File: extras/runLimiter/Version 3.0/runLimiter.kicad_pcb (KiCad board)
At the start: 2 copper layers, 70 x 50 mm, 19 parts, among them J1 5-20 Volts, J2 Vout, J3 Dry Contacts, K1 Relay, Q1 2N3904, Q2 2SD2023, U1 MCP1700-330, U2 ESP8266-01s

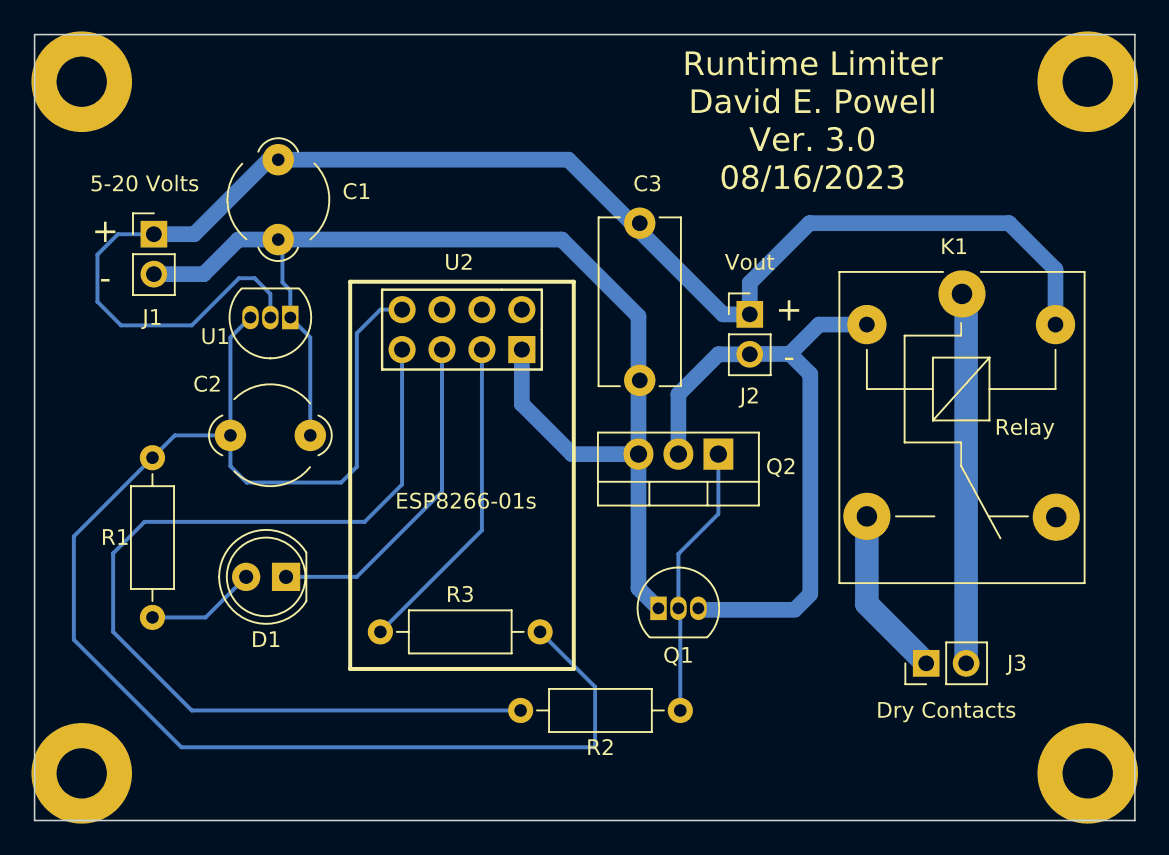
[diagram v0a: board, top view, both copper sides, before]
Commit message: Changes to board and schematic
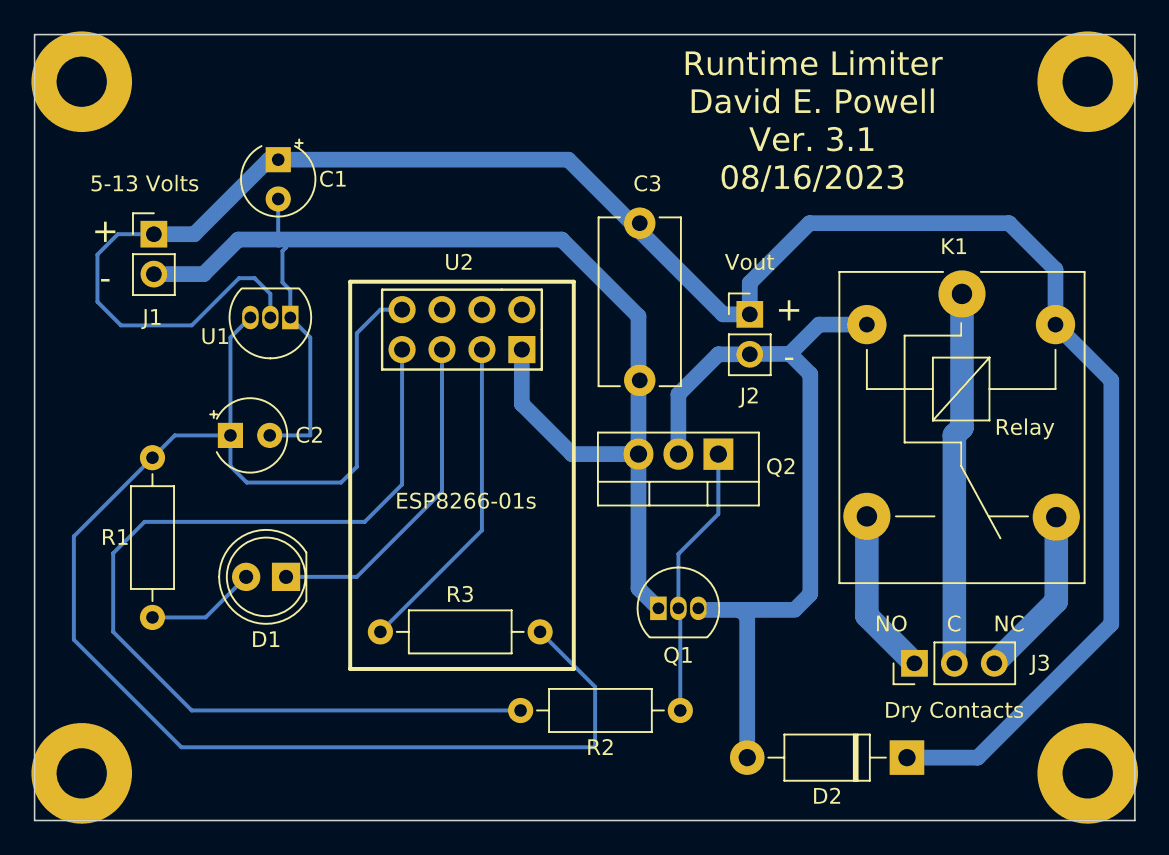
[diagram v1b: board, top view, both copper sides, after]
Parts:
- added D2: 1N4003, Diode_THT:D_DO-41_SOD81_P10.16mm_Horizontal, F.Cu at (55.5, 46.0)
- C1, C2: footprint Ferrite_THT:LairdTech_28C0236-0JW-10 -> Capacitor_THT:CP_Radial_Tantal_D4.5mm_P2.50mm
- J1: value 5-20 Volts -> 5-13 Volts
- J3: footprint Connector_PinHeader_2.54mm:PinHeader_1x02_P2.54mm_Vertical -> Connector_PinHeader_2.54mm:PinHeader_1x03_P2.54mm_Vertical
- moved J3 0.75 mm to (56.0, 40.0)
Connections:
- K1 pad 4: unconnected-(K1-Pad4) -> Net-(K1-Pad4)
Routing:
- net /Control Power: track 94.2 -> 131.3 mm
- net Net-(K1-Pad4): track 0.00 -> 10.9 mm
- net /Control Ground: track 40.8 -> 50.4 mm
- net GNDREF: track 78.6 -> 83.7 mm
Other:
- board text added: "C"
- board text added: "NC"
- board text added: "NO"
- board text added: "Runtime Limiter David E. Powell Ver. 3.1 08/16/2023"
- board text removed: "Runtime Limiter David E. Powell Ver. 3.0 08/16/2023"
